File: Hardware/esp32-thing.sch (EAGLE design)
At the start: 72 parts, among them Q1 2.5A/30V, Q2 MBT3904DW1T1, U1 MCP73831, U3 AP2112K-3.3V, U4 FT231XS, U5 W25Q32FVSS, Y1 26MHz, Y2 32.768kHz

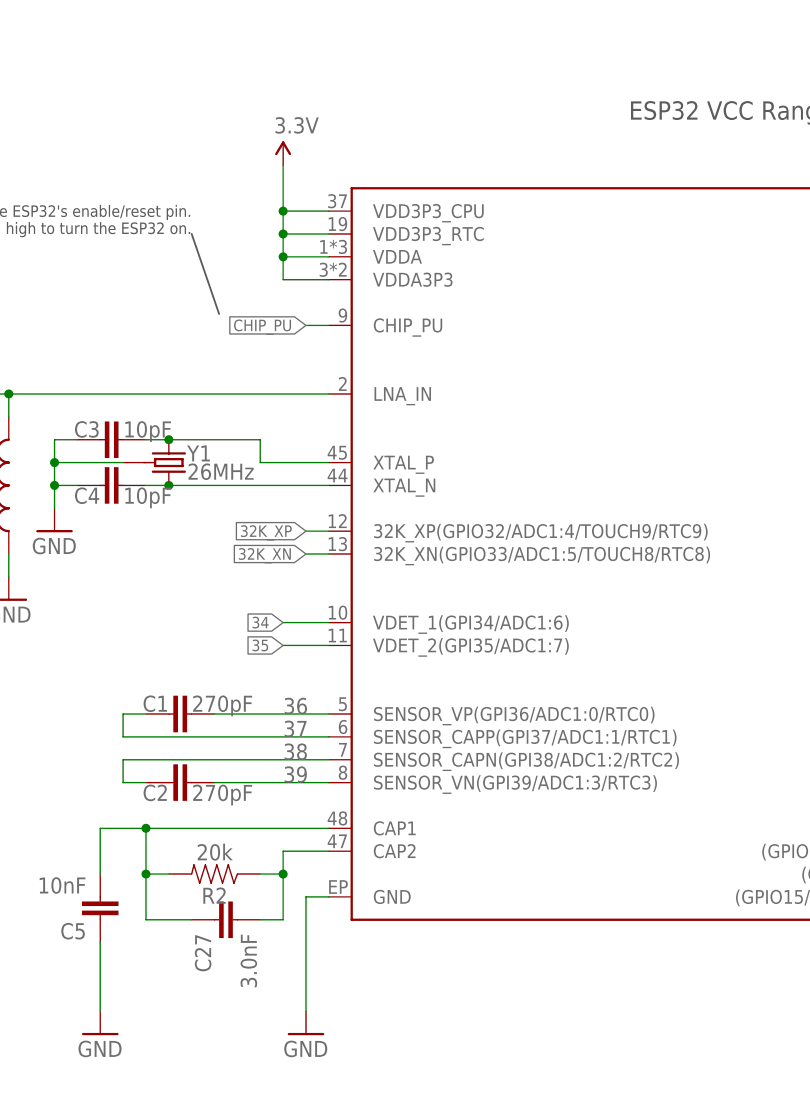
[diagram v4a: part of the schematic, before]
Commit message: Fixing v03 checklist issues.
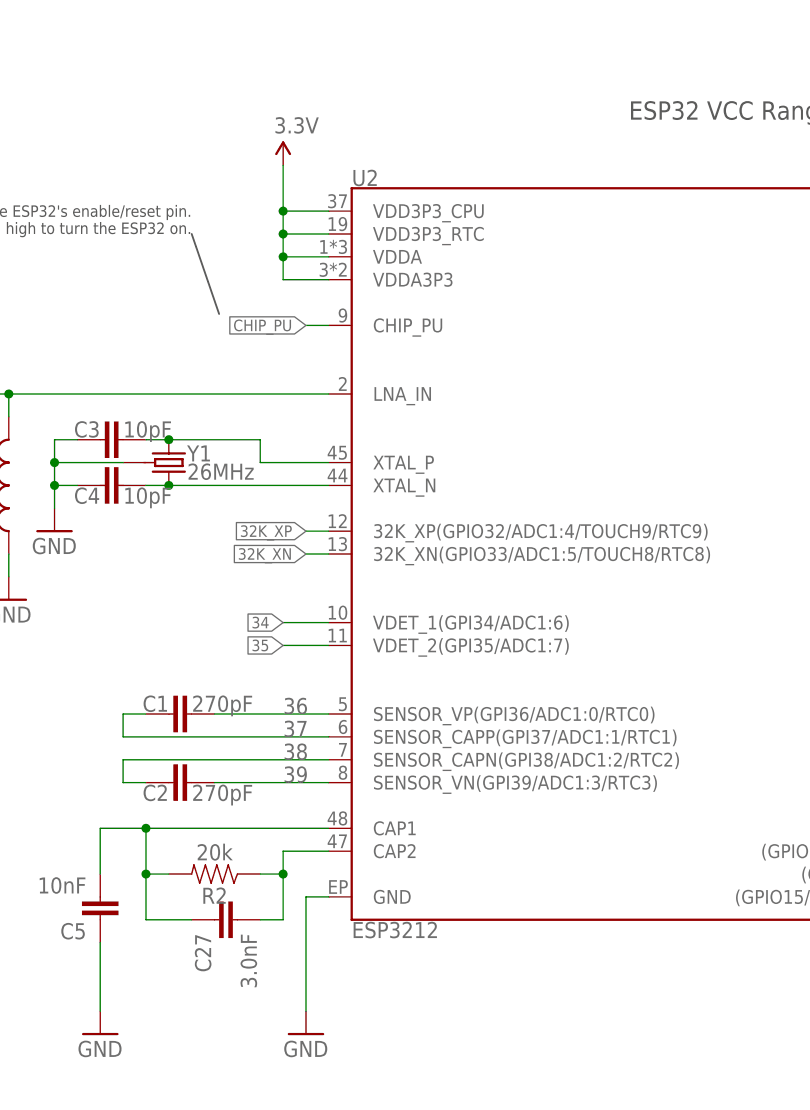
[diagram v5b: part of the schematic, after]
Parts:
- removed U$2: ESP32-2, esp32-thing-temp:ESP32-2
- added U2: ESP3212, esp32-thing-temp:ESP3212
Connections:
- net 0: now also U2.(ADC2:1/TOUCH1/RTC11/CLK_OUT1)GPIO0; no longer U$2.(ADC2:1/TOUCH1/RTC11/CLK_OUT1)GPIO0
- net 12: now also U2.(GPIO12/ADC2:5/TOUCH5/RTC15/SPIQ)MTDI; no longer U$2.(GPIO12/ADC2:5/TOUCH5/RTC15/SPIQ)MTDI
- net 13: now also U2.(GPIO13/ADC2:4/TOUCH4/RTC14/SPID/U0CTS)MTCK; no longer U$2.(GPIO13/ADC2:4/TOUCH4/RTC14/SPID/U0CTS)MTCK
- net 14: now also U2.(GPIO14/ADC2:6/TOUCH6/RTC16/SPICLK)MTMS; no longer U$2.(GPIO14/ADC2:6/TOUCH6/RTC16/SPICLK)MTMS
- net 15: now also U2.(GPIO15/ADC2:3/TOUCH3/RTC13/SPICSO/U0RTS)MTDO; no longer U$2.(GPIO15/ADC2:3/TOUCH3/RTC13/SPICSO/U0RTS)MTDO
- net 16: now also U2.(HS1_DATA4)GPIO16; no longer U$2.(HS1_DATA4)GPIO16
- net 17: now also U2.(HS1_DATA5)GPIO17; no longer U$2.(HS1_DATA5)GPIO17
- net 18: now also U2.(VSPICLK/HS1_DATA7)GPIO18; no longer U$2.(VSPICLK/HS1_DATA7)GPIO18
- net 19: now also U2.(VSPIQ/HS2_DATA2)GPIO19; no longer U$2.(VSPIQ/HS2_DATA2)GPIO19
- net 2: now also U2.(ADC2:2/TOUCH2/RTC12/SPIWP)GPIO2; no longer U$2.(ADC2:2/TOUCH2/RTC12/SPIWP)GPIO2
- net 21: now also U2.(VSPIHD/HS2_CMD)GPIO21; no longer U$2.(VSPIHD/HS2_CMD)GPIO21
- net 22: now also U2.(VSPIWP/HS2_CLK)GPIO22; no longer U$2.(VSPIWP/HS2_CLK)GPIO22
- net 23: now also U2.GPIO23; no longer U$2.GPIO23
- net 25: now also U2.(DAC1/ADC2:8/RTC6)GPIO25; no longer U$2.(DAC1/ADC2:8/RTC6)GPIO25
- net 26: now also U2.(DAC2/ADC2:9/RTC7)GPIO26; no longer U$2.(DAC2/ADC2:9/RTC7)GPIO26
- net 27: now also U2.(ADC2:7/TOUCH7/RTC17)GPIO27; no longer U$2.(ADC2:7/TOUCH7/RTC17)GPIO27
- net 3.3V: now also U2.VDD3P3_CPU, U2.VDD3P3_RTC, U2.VDDA, U2.VDDA3P3; no longer U$2.VDD3P3_CPU, U$2.VDD3P3_RTC, U$2.VDDA, U$2.VDDA3P3
- net 32K_XN: now also U2.32K_XN(GPIO33/ADC1:5/TOUCH8/RTC8); no longer U$2.32K_XN(GPIO33/ADC1:5/TOUCH8/RTC8)
- net 32K_XP: now also U2.32K_XP(GPIO32/ADC1:4/TOUCH9/RTC9); no longer U$2.32K_XP(GPIO32/ADC1:4/TOUCH9/RTC9)
- net 34: now also U2.VDET_1(GPI34/ADC1:6); no longer U$2.VDET_1(GPI34/ADC1:6)
- net 35: now also U2.VDET_2(GPI35/ADC1:7); no longer U$2.VDET_2(GPI35/ADC1:7)
- net 36: now also U2.SENSOR_VP(GPI36/ADC1:0/RTC0); no longer U$2.SENSOR_VP(GPI36/ADC1:0/RTC0)
- net 37: now also U2.SENSOR_CAPP(GPI37/ADC1:1/RTC1); no longer U$2.SENSOR_CAPP(GPI37/ADC1:1/RTC1)
- net 38: now also U2.SENSOR_CAPN(GPI38/ADC1:2/RTC2); no longer U$2.SENSOR_CAPN(GPI38/ADC1:2/RTC2)
- net 39: now also U2.SENSOR_VN(GPI39/ADC1:3/RTC3); no longer U$2.SENSOR_VN(GPI39/ADC1:3/RTC3)
- net 4: now also U2.(ADC2:0/TOUCH0/RTC10/SPIHD)GPIO4; no longer U$2.(ADC2:0/TOUCH0/RTC10/SPIHD)GPIO4
- net 5: now also U2.(VSPICS0/HS1_DATA6)GPIO5; no longer U$2.(VSPICS0/HS1_DATA6)GPIO5
- net CAP_10N: now also U2.CAP1; no longer U$2.CAP1
- net CHIP_PU: now also U2.CHIP_PU; no longer U$2.CHIP_PU
- net FLASH_SCK: now also U2.(GPIO6/SPICLK/HS1_CLK/U1CTS)SD_CLK; no longer U$2.(GPIO6/SPICLK/HS1_CLK/U1CTS)SD_CLK
- net FLASH_SCS: now also U2.(GPIO11/SPICSO/HS1_CMD/U1RTS)SD_CMD; no longer U$2.(GPIO11/SPICSO/HS1_CMD/U1RTS)SD_CMD
- net FLASH_SDI: now also U2.(GPIO8/SPID/HS1_DATA1)SD_DATA1; no longer U$2.(GPIO8/SPID/HS1_DATA1)SD_DATA1
- net FLASH_SDO: now also U2.(GPIO7/SPI1/HS1_DATA0)SD_DATA0; no longer U$2.(GPIO7/SPI1/HS1_DATA0)SD_DATA0
- net FLASH_SHD: now also U2.(GPIO9/SPIHD/HS1_DATA2/U1RX)SD_DATA2; no longer U$2.(GPIO9/SPIHD/HS1_DATA2/U1RX)SD_DATA2
- net FLASH_SWP: now also U2.(GPIO10/SPIWP/HS1_DATA3/U1TX)SD_DATA3; no longer U$2.(GPIO10/SPIWP/HS1_DATA3/U1TX)SD_DATA3
- net FLASH_VDD: now also U2.VDD3P3_SDIO; no longer U$2.VDD3P3_SDIO
- net GND: now also U2.GND; no longer U$2.GND
- net LNA_IN: now also U2.LNA_IN; no longer U$2.LNA_IN
- net N$13: now also U2.XTAL_P; no longer U$2.XTAL_P
- net N$15: now also U2.XTAL_N; no longer U$2.XTAL_N
- net N$4: now also U2.CAP2; no longer U$2.CAP2
- net U0RXD: now also U2.(GPIO3/CLK_OUT2/HS2_DATA0)U0RXD; no longer U$2.(GPIO3/CLK_OUT2/HS2_DATA0)U0RXD
- net U0TXD: now also U2.(GPIO1/CLK_OUT3/HS2_DATA1)U0TXD; no longer U$2.(GPIO1/CLK_OUT3/HS2_DATA1)U0TXD

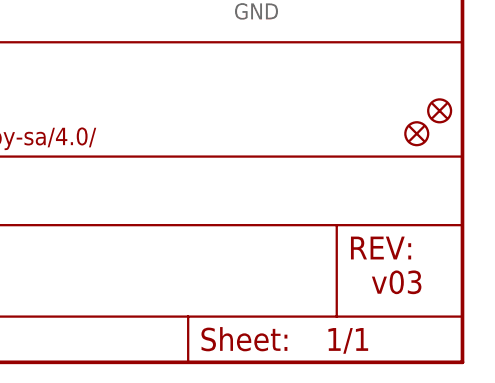
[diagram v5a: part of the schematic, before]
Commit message: Upping to v10, fixing some silk.
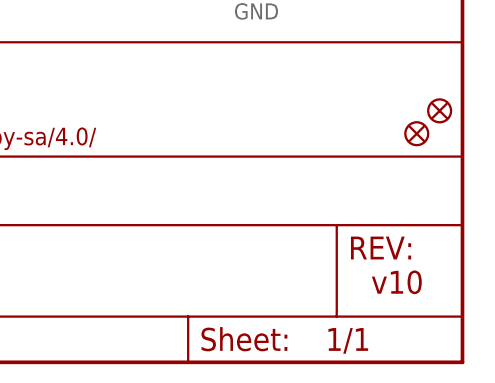
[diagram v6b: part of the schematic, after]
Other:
- note added: "v10"
- note removed: "v03"
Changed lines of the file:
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@@
 <?xml version="1.0" encoding="utf-8"?>
 <!DOCTYPE eagle SYSTEM "eagle.dtd">
-<eagle version="7.6.0">
+<eagle version="7.5.0">
 <drawing>
 <settings>
@@
 <text x="200.66" y="53.34" size="2.54" layer="94" align="top-left">GPIO5 LED</text>
 <text x="332.74" y="104.14" size="2.54" layer="94" align="top-left">Headers</text>
-<text x="421.64" y="10.16" size="2.54" layer="94" align="top-left">v03</text>
+<text x="421.64" y="10.16" size="2.54" layer="94" align="top-left">v10</text>
 <text x="354.838" y="11.43" size="2.54" layer="94" rot="MR180" align="top-left">Jim Lindblom</text>
 <text x="124.46" y="165.1" size="2.032" layer="97" font="vector" align="bottom-center">ESP32 VCC Range: 2.8-3.6V</text>
